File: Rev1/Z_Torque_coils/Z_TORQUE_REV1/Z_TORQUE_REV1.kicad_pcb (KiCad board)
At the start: 4 copper layers, 95.9 x 90.2 mm, 50 parts, among them IC1 MPM3610AGQV-Z, J1 F3311A7H121014E200, J2 F3311A7H121014E200, Q1 BSS138, Q2 BSS138, Q3 MBT2222ADW1T1, Q4 BSS138, Q5 BSS138, Q6 MBT2222ADW1T1, U1 DRV8830DGQ

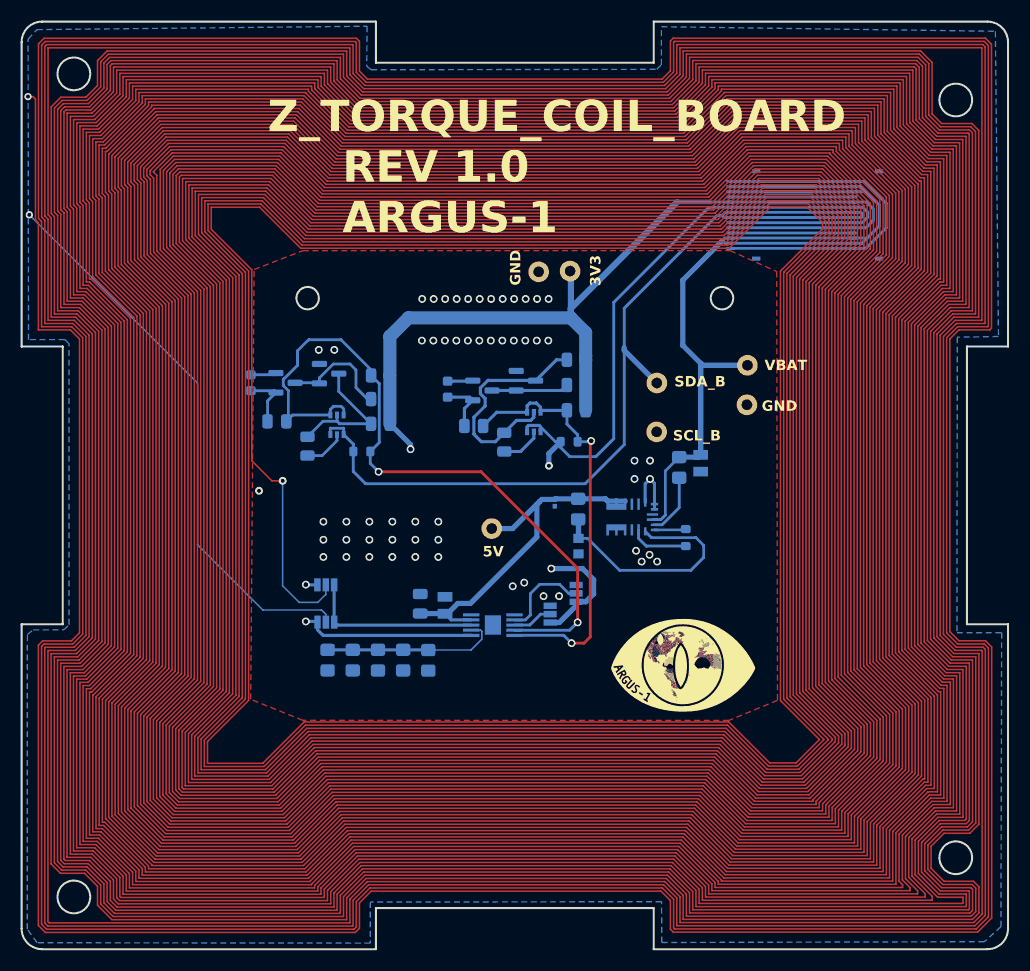
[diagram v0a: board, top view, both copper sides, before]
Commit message: Changed orientation of Z Torque
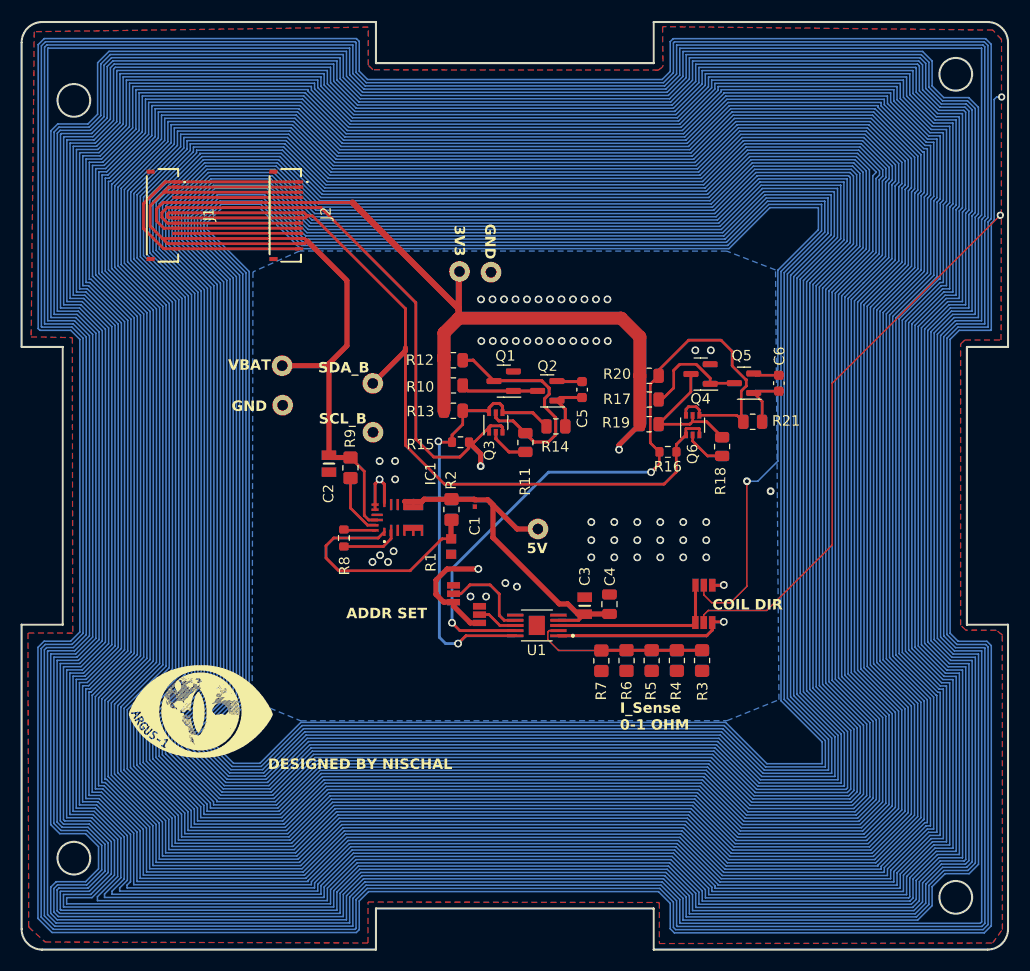
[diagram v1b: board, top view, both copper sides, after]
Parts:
- ., C1, C2, C3, C4, C5, C6, IC1, J1, J2, JP1, JP2, JP3, JP4, Q1, Q2, Q3, Q4, Q5, Q6, R1, R10, R11, R12, R13, R14, R15, R16, R17, R18, R19, R2, R20, R21, R3, R4, R5, R6, R7, R8, R9, U1: moved to F.Cu
- ., ? (x7): moved to B.Cu
- moved J1 68.5 mm to (118.2, 66.4)
- moved . 61.5 mm to (121.7, 114.6), turned to 0 degrees
- moved C6 51.3 mm to (178.1, 82.7)
- moved R21 46.3 mm to (175.6, 86.5), turned to 180 degrees
- moved ? 45.2 mm to (129.9, 81.0), turned to 180 degrees
- moved ? 45.1 mm to (129.9, 84.9), turned to 180 degrees
- moved J2 44.6 mm to (130.2, 66.4)
- moved Q5 44.6 mm to (174.8, 82.7), turned to 180 degrees
- moved R18 40.3 mm to (172.6, 88.9)
- moved JP4 36.8 mm to (170.9, 102.4), turned to 0 degrees
- moved JP3 36.7 mm to (170.8, 106.0), turned to 180 degrees
- moved R3 36.4 mm to (170.7, 109.7)
- moved C2 36.1 mm to (134.4, 90.6)
- moved Q4 36.1 mm to (170.5, 81.8), turned to 180 degrees
- moved Q6 34.6 mm to (169.8, 86.8)
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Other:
- outline, holes or cut-outs redrawn

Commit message: made changes to step
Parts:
- ., ? (x7): moved to F.Cu
- ., C1, C2, C3, C4, C5, C6, IC1, J1, J2, JP1, JP2, JP3, JP4, Q1, Q2, Q3, Q4, Q5, Q6, R1, R10, R11, R12, R13, R14, R15, R16, R17, R18, R19, R2, R20, R21, R3, R4, R5, R6, R7, R8, R9, U1: moved to B.Cu
- moved . 61.7 mm to (179.0, 65.6), turned to 0 degrees
- moved . 61.5 mm to (183.2, 114.6), turned to 180 degrees
- moved ? 41.7 mm to (147.1, 113.5)
- moved ? 41.5 mm to (150.2, 113.5)
- moved R7 34.0 mm to (160.9, 75.7), turned to 90 degrees
- moved R3 34.0 mm to (170.7, 75.7), turned to 90 degrees
- moved R4 34.0 mm to (168.2, 75.7), turned to 90 degrees
- moved R5 34.0 mm to (165.8, 75.7), turned to 90 degrees
- moved R6 34.0 mm to (163.3, 75.7), turned to 90 degrees
- moved U1 27.2 mm to (154.6, 79.1)
- moved JP3 26.6 mm to (170.8, 79.4)
- moved JP1 25.0 mm to (149.0, 80.2), turned to 90 degrees
- moved R12 24.4 mm to (146.5, 104.9)
- moved C3 23.3 mm to (159.3, 81.1), turned to 90 degrees
- moved C4 23.0 mm to (161.7, 81.2), turned to -90 degrees
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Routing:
- net +3.3V: track 126.2 -> 187.0 mm, vias 2 -> 3
- net GND: track 34.5 -> 54.6 mm, vias 56 -> 62
- net SCL1_b4iso: track 82.4 -> 101.7 mm, vias 1 -> 2
- net coils: track 50068.4 -> 50079.3 mm
- net SDA1_b4iso: track 94.0 -> 103.0 mm, vias 0 -> 1
- net VBATT: track 98.2 -> 104.2 mm, vias 0 -> 1
- net SCL_TORQUE: track 42.0 -> 43.3 mm
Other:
- outline, holes or cut-outs redrawn
- board text added: "1"
- board text added: "2"
- board text added: "A0"
- board text added: "A1"
- board text added: "TR"
